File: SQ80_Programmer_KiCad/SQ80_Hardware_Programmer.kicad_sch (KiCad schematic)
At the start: 50 parts, among them J1 MIDI IN, J2 MIDI OUT/THRU, SW1 ARCH_MODE, SW2 GLITCH_TRIG, U1 MUX_1, U2 MUX_2, U3 6N138, U4 ER_OLEDM0.91_1x-I2C

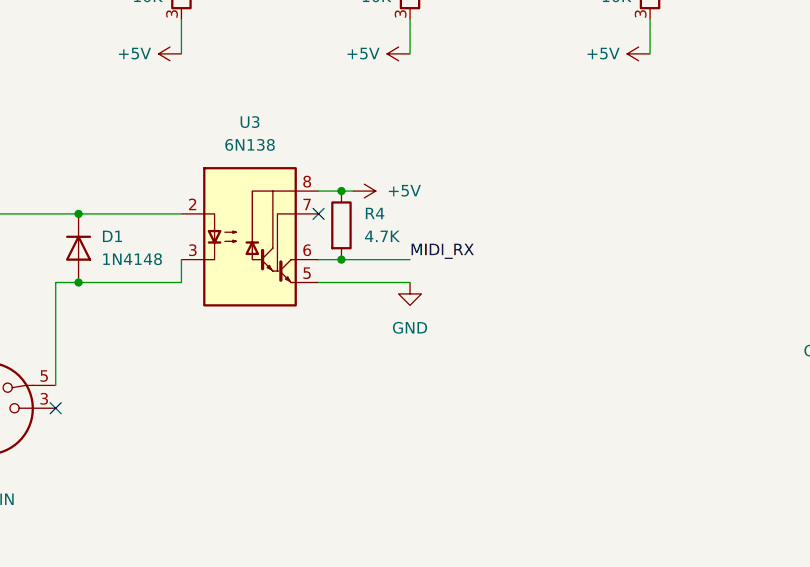
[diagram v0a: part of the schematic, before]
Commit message: PCB and Readme Updates
Added functional descriptions for SW1 and SW2 in README.  Update PCB to add R5 to MIDI input section.
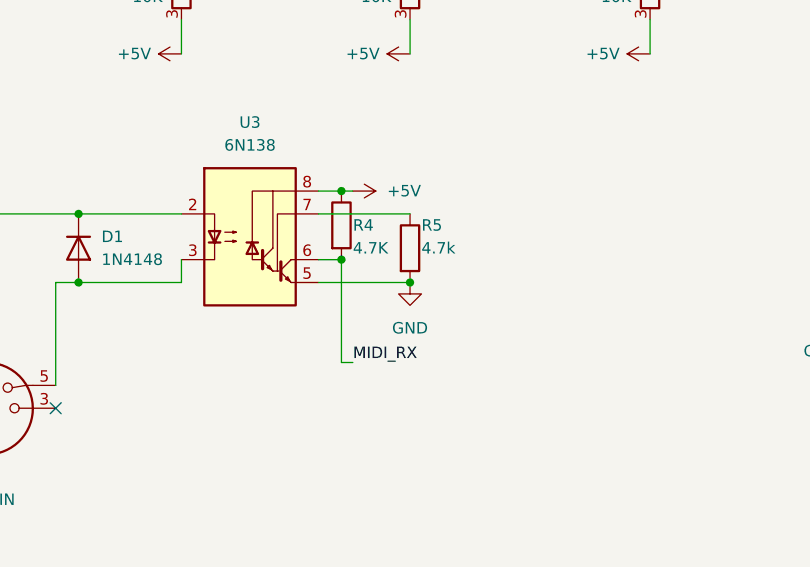
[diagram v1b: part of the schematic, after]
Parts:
- added R5: 4.7k, Resistor_THT:R_Axial_DIN0207_L6.3mm_D2.5mm_P15.24mm_Horizontal, symbol Device:R
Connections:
- net GND: now also R5.2
- net at U3.7 (VO1): now also R5.1
- no-connect marks 21 -> 20
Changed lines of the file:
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@@
 	)
 	(junction
+		(at 191.77 134.62)
+		(diameter 0)
+		(color 0 0 0 0)
+	)
+	(junction
 		(at 154.94 127)
 		(diameter 0)
@@
 	)
 	(no_connect
-		(at 181.61 127)
-	)
-	(no_connect
 		(at 137.16 148.59)
 	)
@@
 	(wire
 		(pts
+			(xy 181.61 127) (xy 191.77 127)
+		)
+		(stroke
+			(width 0)
+			(type default)
+		)
+	)
+	(wire
+		(pts
 			(xy 237.49 119.38) (xy 243.84 119.38)
 		)
@@
 	(wire
 		(pts
+			(xy 184.15 143.51) (xy 185.42 143.51)
+		)
+		(stroke
+			(width 0)
+			(type default)
+		)
+	)
+	(wire
+		(pts
 			(xy 170.18 101.6) (xy 171.45 101.6)
 		)
@@
 	(wire
 		(pts
+			(xy 184.15 132.08) (xy 184.15 143.51)
+		)
+		(stroke
+			(width 0)
+			(type default)
+		)
+	)
+	(wire
+		(pts
 			(xy 91.44 68.58) (xy 90.17 68.58)
 		)
@@
 		)
 	)
-	(wire
-		(pts
-			(xy 184.15 132.08) (xy 191.77 132.08)
-		)
-		(stroke
-			(width 0)
-			(type default)
-		)
-	)
 	(label "POT_27"
 		(at 96.52 101.6 0)
@@
 	)
 	(label "MIDI_RX"
-		(at 191.77 132.08 0)
+		(at 185.42 143.51 0)
 		(effects
 			(font
@@
 		(in_pos_files yes)
 		(dnp no)
-		(fields_autoplaced yes)
 		(property "Reference" "R4"
-			(at 186.69 126.9999 0)
+			(at 185.42 128.27 0)
 			(show_name no)
 			(do_not_autoplace no)
@@
 		)
 		(property "Value" "4.7K"
-			(at 186.69 129.5399 0)
+			(at 185.42 130.81 0)
 			(show_name no)
 			(do_not_autoplace no)
@@
 					(unit 1)
 				)
+			)
+		)
+	)
+	(symbol
+		(lib_id "Device:R")
+		(at 191.77 130.81 0)
+		(unit 1)
+		(body_style 1)
+		(exclude_from_sim no)
+		(in_bom yes)
+		(on_board yes)
+		(in_pos_files yes)
+		(dnp no)
+		(property "Reference" "R5"
+			(at 193.04 128.27 0)
+			(show_name no)
+			(do_not_autoplace no)
+			(effects
+				(font
+					(size 1.27 1.27)
+				)
+				(justify left)
+			)
+		)
+		(property "Value" "4.7k"
+			(at 193.04 130.81 0)
+			(show_name no)
+			(do_not_autoplace no)
+			(effects
+				(font
+					(size 1.27 1.27)
+				)
+				(justify left)
+			)
+		)
+		(property "Footprint" "Resistor_THT:R_Axial_DIN0207_L6.3mm_D2.5mm_P15.24mm_Horizontal"
+			(at 189.992 130.81 90)
+			(hide yes)
+			(show_name no)
+			(do_not_autoplace no)
+			(effects
+				(font
+					(size 1.27 1.27)
+				)
+			)
+		)
+		(property "Datasheet" ""
+			(at 191.77 130.81 0)
+			(hide yes)
+			(show_name no)
+			(do_not_autoplace no)
+			(effects
+				(font
+					(size 1.27 1.27)
+				)
+			)
+		)
+		(property "Description" "Resistor"
+			(at 191.77 130.81 0)
+			(hide yes)
+			(show_name no)
+			(do_not_autoplace no)
+			(effects
+				(font
+					(size 1.27 1.27)
+				)
+			)
+		)
+		(pin "2"
+		)
+		(pin "1"
+		)
+		(instances
+			(project "SQ80_Hardware_Programmer"
+				(path "/0a1bab55-9cef-453b-9c94-64f0d74b9412"
+					(reference "R5")
+					(unit 1)
+				)
